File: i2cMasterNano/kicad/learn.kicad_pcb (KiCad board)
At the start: 2 copper layers, 28 parts, among them J1 Conn_01x04_Male, J10 Conn_01x01, J2 Conn_01x04_Male, J3 Conn_01x04_Male, J4 Conn_01x04_Male, J5 Conn_01x04_Male, J6 Conn_01x04_Male, J7 Conn_01x04_Male, J8 Conn_01x04_Male, J9 Conn_01x01, SW1 SW_DIP_x04, U1 LM7805_TO220, U2 Arduino_Nano_R3

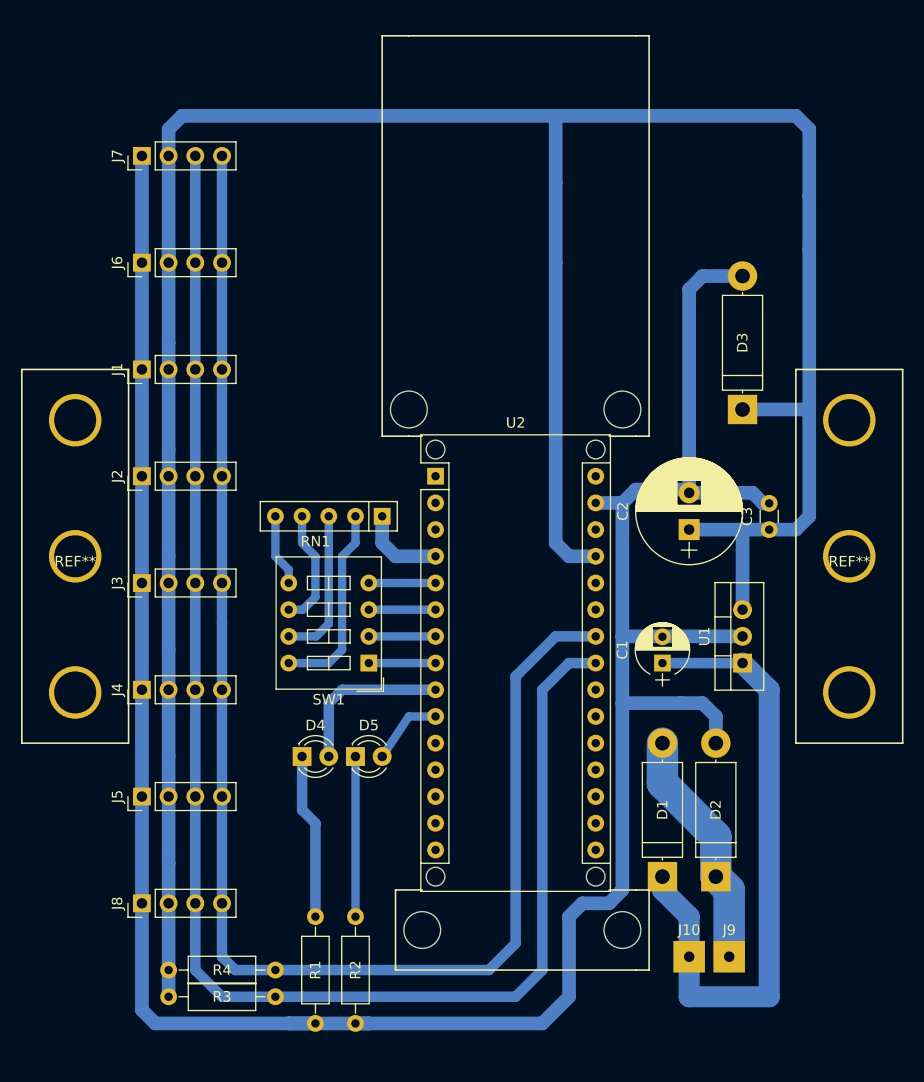
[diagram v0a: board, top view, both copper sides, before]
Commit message: 3pin dip switch due to D4 occupied by wiznet shield
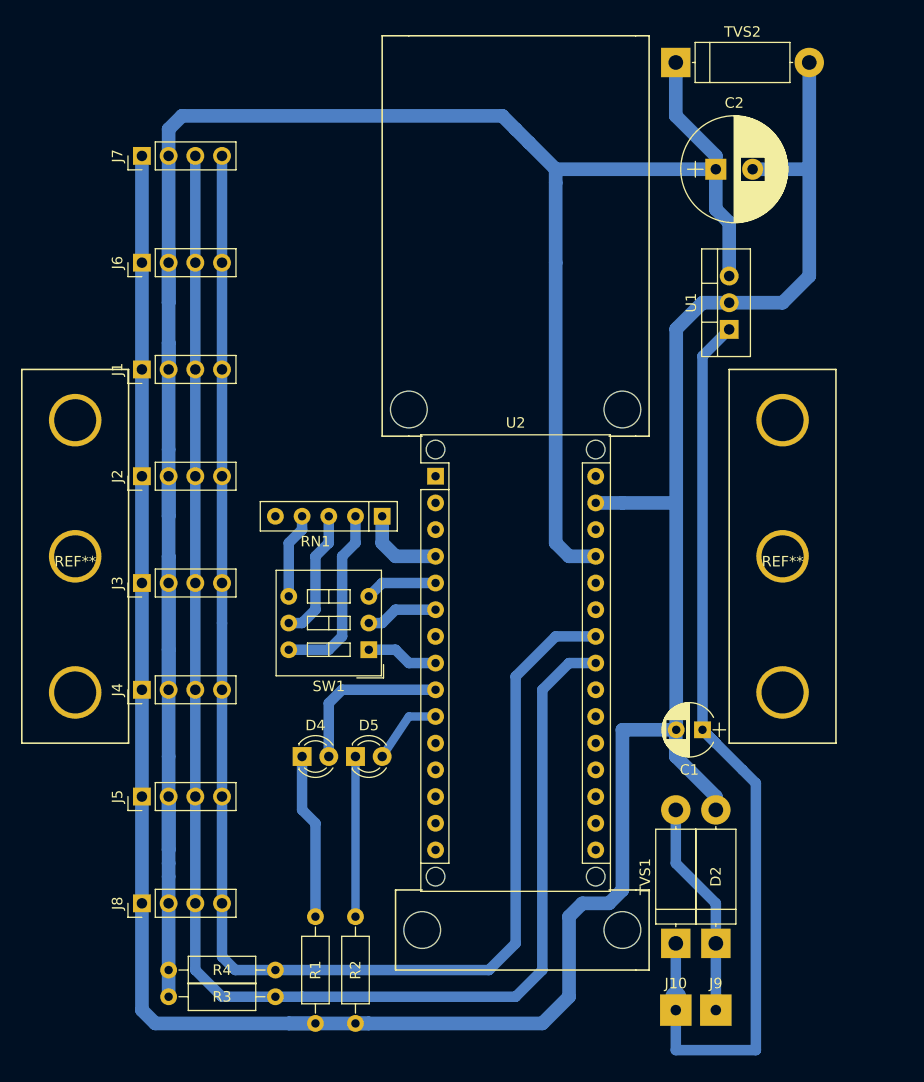
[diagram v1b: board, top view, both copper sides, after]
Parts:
- removed C3: 100nF, Capacitors_THT:C_Disc_D3.0mm_W1.6mm_P2.50mm
- removed D1, D3: D_TVS, Diodes_THT:D_5W_P12.70mm_Horizontal
- added TVS1: D_TVS, Diodes_THT:D_5W_P12.70mm_Horizontal, F.Cu at (191.8, 153.7)
- added TVS2: D_TVS, Diodes_THT:D_5W_P12.70mm_Horizontal, F.Cu at (191.8, 69.8)
- SW1: value SW_DIP_x04 -> SW_DIP_x03; footprint Buttons_Switches_THT:SW_DIP_x4_W7.62mm_Slide -> Buttons_Switches_THT:SW_DIP_x3_W7.62mm_Slide
- moved C2 34.4 mm to (195.6, 80.0), turned to 0 degrees
- moved U1 31.8 mm to (196.8, 95.2)
- moved C1 7.41 mm to (194.3, 133.3), turned to 180 degrees
- moved D2 6.35 mm to (195.6, 153.7)
- moved REF** 6.35 mm to (201.9, 116.8)
- moved J10 5.24 mm to (193.0, 158.8)
- moved J9 5.24 mm to (196.8, 158.8)
- moved SW1 1.27 mm to (162.6, 125.7)
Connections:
- SW1 pad 4: Net-(SW1-Pad4) -> Net-(RN1-Pad4)
- SW1 pad 5: Net-(RN1-Pad5) -> Net-(RN1-Pad3)
- SW1 pad 6: Net-(RN1-Pad4) -> Net-(RN1-Pad2)
- U2 pad 7: Net-(SW1-Pad3) -> Net-(U2-Pad7)
- U2 pad 8: Net-(SW1-Pad4) -> Net-(SW1-Pad3)
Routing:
- net Net-(C1-Pad1): track 60.5 -> 92.6 mm
- net +5V: track 253.6 -> 230.1 mm
- net Net-(D2-Pad1): track 33.9 -> 20.6 mm
- net GND: track 253.4 -> 265.1 mm
- net Net-(RN1-Pad5): track 6.88 -> 0.00 mm
- net Net-(SW1-Pad4): track 6.35 -> 0.00 mm
- net Net-(RN1-Pad4): track 11.3 -> 8.15 mm
- net Net-(RN1-Pad3): track 14.5 -> 12.5 mm
- net Net-(RN1-Pad2): track 18.8 -> 17.6 mm
- net Net-(SW1-Pad1): track 6.35 -> 6.88 mm
- net Net-(SW1-Pad2): track 6.35 -> 6.88 mm
- net Net-(SW1-Pad3): track 6.35 -> 6.88 mm

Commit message: ...
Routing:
- net GND: track 265.1 -> 263.6 mm
- net Net-(C1-Pad1): track 92.6 -> 91.2 mm
- net +5V: track 230.1 -> 229.3 mm
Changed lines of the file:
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@@
     (links 63)
     (no_connects 1)
-    (area 129.064999 65.765 213.460001 165.200001)
+    (area 129.064999 65.765 207.485001 165.230002)
     (thickness 1.6)
     (drawings 6)
-    (tracks 163)
+    (tracks 165)
     (zones 0)
     (modules 27)
@@
   )
   (setup
-    (last_trace_width 1)
+    (last_trace_width 2)
     (user_trace_width 1)
     (user_trace_width 2)
@@
   (gr_line (start 207.01 66.04) (end 207.01 111.76) (angle 90) (layer Margin) (width 0.2))
   (gr_line (start 129.54 163.83) (end 129.54 66.04) (angle 90) (layer Margin) (width 0.2))
+  (segment (start 187.96 134.62) (end 189.23 133.35) (width 1.3) (layer B.Cu) (net 1))
   (segment (start 199.08 80.01) (end 204.47 80.01) (width 1.3) (layer B.Cu) (net 1))
   (segment (start 196.85 92.71) (end 201.93 92.71) (width 1.3) (layer B.Cu) (net 1))
@@
   (segment (start 204.47 80.01) (end 204.47 69.85) (width 1.3) (layer B.Cu) (net 1))
   (segment (start 201.93 92.71) (end 204.47 90.17) (width 1.3) (layer B.Cu) (net 1))
-  (segment (start 191.81 133.35) (end 186.69 133.35) (width 1.3) (layer B.Cu) (net 1))
+  (segment (start 191.81 133.35) (end 189.23 133.35) (width 1.3) (layer B.Cu) (net 1))
   (segment (start 186.69 111.76) (end 191.81 111.76) (width 1.3) (layer B.Cu) (net 1))
   (segment (start 191.81 111.76) (end 191.77 111.76) (width 1.3) (layer B.Cu) (net 1))
@@
   (segment (start 161.29 161.29) (end 162.56 161.29) (width 1.3) (layer B.Cu) (net 1))
   (segment (start 157.48 161.29) (end 154.94 161.29) (width 1.3) (layer B.Cu) (net 1) (status 10))
-  (segment (start 186.69 133.35) (end 186.69 148.59) (width 1.3) (layer B.Cu) (net 1))
-  (segment (start 186.69 148.59) (end 185.42 149.86) (width 1.3) (layer B.Cu) (net 1))
+  (segment (start 187.96 134.62) (end 187.96 147.32) (width 1.3) (layer B.Cu) (net 1))
+  (segment (start 187.96 147.32) (end 185.42 149.86) (width 1.3) (layer B.Cu) (net 1))
   (segment (start 185.42 149.86) (end 182.88 149.86) (width 1.3) (layer B.Cu) (net 1))
   (segment (start 182.88 149.86) (end 181.61 151.13) (width 1.3) (layer B.Cu) (net 1))
@@
   (segment (start 163.83 115.57) (end 165.1 116.84) (width 1.3) (layer B.Cu) (net 1))
   (segment (start 184.15 111.76) (end 186.69 111.76) (width 1.3) (layer B.Cu) (net 1) (status 10))
-  (segment (start 175.26 74.93) (end 176.53 76.2) (width 1.3) (layer B.Cu) (net 2))
-  (segment (start 177.8 77.47) (end 180.34 80.01) (width 1.3) (layer B.Cu) (net 2))
-  (segment (start 176.53 76.2) (end 177.8 77.47) (width 1.3) (layer B.Cu) (net 2))
-  (segment (start 195.58 80.01) (end 180.34 80.01) (width 1.3) (layer B.Cu) (net 2))
+  (segment (start 180.34 80.01) (end 180.34 74.93) (width 1.3) (layer B.Cu) (net 2))
+  (segment (start 175.26 74.93) (end 180.34 74.93) (width 1.3) (layer B.Cu) (net 2))
+  (segment (start 180.34 74.93) (end 191.77 74.93) (width 1.3) (layer B.Cu) (net 2))
   (segment (start 195.58 80.01) (end 195.58 78.74) (width 1.3) (layer B.Cu) (net 2))
   (segment (start 195.58 78.74) (end 191.77 74.93) (width 1.3) (layer B.Cu) (net 2))
@@
   (segment (start 176.53 128.27) (end 176.53 153.67) (width 1) (layer B.Cu) (net 4))
   (segment (start 180.34 124.46) (end 176.53 128.27) (width 1) (layer B.Cu) (net 4))
-  (segment (start 196.85 95.25) (end 194.31 97.79) (width 1) (layer B.Cu) (net 24))
-  (segment (start 194.31 97.79) (end 194.31 133.35) (width 1) (layer B.Cu) (net 24))
-  (segment (start 194.31 133.35) (end 195.58 134.62) (width 1) (layer B.Cu) (net 24))
-  (segment (start 198.12 137.16) (end 199.39 138.43) (width 1) (layer B.Cu) (net 24))
-  (segment (start 191.77 160.02) (end 191.77 163.83) (width 1) (layer B.Cu) (net 24))
-  (segment (start 191.77 163.83) (end 199.39 163.83) (width 1) (layer B.Cu) (net 24))
-  (segment (start 199.39 163.83) (end 199.39 138.43) (width 1) (layer B.Cu) (net 24))
-  (segment (start 198.12 137.16) (end 195.58 134.62) (width 1) (layer B.Cu) (net 24))
-  (segment (start 195.58 134.62) (end 194.31 133.35) (width 1) (layer B.Cu) (net 24))
-  (segment (start 191.77 160.02) (end 191.77 153.67) (width 1) (layer B.Cu) (net 24))
+  (segment (start 196.85 135.89) (end 196.85 133.35) (width 2) (layer B.Cu) (net 24))
+  (segment (start 194.31 133.35) (end 195.58 133.35) (width 2) (layer B.Cu) (net 24))
+  (segment (start 195.58 133.35) (end 196.85 133.35) (width 2) (layer B.Cu) (net 24))
+  (segment (start 196.85 95.25) (end 196.85 97.79) (width 2) (layer B.Cu) (net 24))
+  (segment (start 196.85 97.79) (end 196.85 132.08) (width 2) (layer B.Cu) (net 24))
+  (segment (start 196.85 132.08) (end 196.85 133.35) (width 2) (layer B.Cu) (net 24))
+  (segment (start 198.12 137.16) (end 199.39 138.43) (width 2) (layer B.Cu) (net 24))
+  (segment (start 191.77 160.02) (end 191.77 163.83) (width 2) (layer B.Cu) (net 24))
+  (segment (start 191.77 163.83) (end 199.39 163.83) (width 2) (layer B.Cu) (net 24))
+  (segment (start 199.39 163.83) (end 199.39 138.43) (width 2) (layer B.Cu) (net 24))
+  (segment (start 198.12 137.16) (end 196.85 135.89) (width 2) (layer B.Cu) (net 24))
+  (segment (start 191.77 160.02) (end 191.77 153.67) (width 2) (layer B.Cu) (net 24))
   (segment (start 191.77 160.02) (end 191.77 158.75) (width 2) (layer B.Cu) (net 24) (status 30))
   (segment (start 196.85 95.25) (end 196.85 95.25) (width 2) (layer B.Cu) (net 24) (status 30))
@@
   (segment (start 168.91 132.08) (end 166.37 132.08) (width 0.8) (layer B.Cu) (net 35))
   (segment (start 166.37 132.08) (end 163.83 135.89) (width 0.8) (layer B.Cu) (net 35) (status 20))
-  (segment (start 195.58 153.67) (end 195.58 149.86) (width 1) (layer B.Cu) (net 36))
-  (segment (start 191.77 146.05) (end 191.77 140.97) (width 1) (layer B.Cu) (net 36))
-  (segment (start 195.58 149.86) (end 191.77 146.05) (width 1) (layer B.Cu) (net 36))
-  (segment (start 195.58 160.02) (end 195.58 153.67) (width 1) (layer B.Cu) (net 36))
+  (segment (start 195.58 153.67) (end 195.58 149.86) (width 3) (layer B.Cu) (net 36))
+  (segment (start 191.77 146.05) (end 191.77 140.97) (width 3) (layer B.Cu) (net 36))
+  (segment (start 195.58 149.86) (end 191.77 146.05) (width 3) (layer B.Cu) (net 36))
+  (segment (start 195.58 160.02) (end 195.58 153.67) (width 3) (layer B.Cu) (net 36))
 )
